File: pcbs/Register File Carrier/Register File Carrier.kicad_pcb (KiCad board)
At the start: 2 copper layers, 4 parts, among them J1001 Conn_02x20_Odd_Even, J1002 Conn_02x20_Odd_Even

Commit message: Roughing a little more out
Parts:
- added J2003: ~, BoardEdgeConnectors:TE-5530843-4-Mount, F.Cu at (151.1, 118.7)
- added J2004: ~, BoardEdgeConnectors:TE-5530843-4-Mount, F.Cu at (148.6, 70.5)
- added U2001: 74AHC04, Package_SO:SOIC-14_3.9x8.7mm_P1.27mm, F.Cu at (109.2, 127.0)
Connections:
- J1001 pad 10: /A7 -> /Connector Block/A7
- J1001 pad 11: /A8 -> /Connector Block/A8
- J1001 pad 12: /A9 -> /Connector Block/A9
- J1001 pad 13: /A10 -> /Connector Block/A10
- J1001 pad 14: /A11 -> /Connector Block/A11
- J1001 pad 15: /A12 -> /Connector Block/A12
- J1001 pad 16: /A13 -> /Connector Block/A13
- J1001 pad 17: /A14 -> /Connector Block/A14
- J1001 pad 18: /A15 -> /Connector Block/A15
- J1001 pad 19: /B0 -> /Connector Block/B0
- J1001 pad 20: /B1 -> /Connector Block/B1
- J1001 pad 21: /B2 -> /Connector Block/B2
- J1001 pad 22: /B3 -> /Connector Block/B3
- J1001 pad 23: /B4 -> /Connector Block/B4
- J1001 pad 24: /B5 -> /Connector Block/B5
- J1001 pad 25: /B6 -> /Connector Block/B6
- J1001 pad 26: /B7 -> /Connector Block/B7
- J1001 pad 27: /B8 -> /Connector Block/B8
- J1001 pad 28: /B9 -> /Connector Block/B9
- J1001 pad 29: /B10 -> /Connector Block/B10
- J1001 pad 3: /A0 -> /Connector Block/A0
- J1001 pad 30: /B11 -> /Connector Block/B11
- J1001 pad 31: /B12 -> /Connector Block/B12
- J1001 pad 32: /B13 -> /Connector Block/B13
- J1001 pad 33: /B14 -> /Connector Block/B14
- J1001 pad 34: /B15 -> /Connector Block/B15
- J1001 pad 4: /A1 -> /Connector Block/A1
- J1001 pad 5: /A2 -> /Connector Block/A2
- J1001 pad 6: /A3 -> /Connector Block/A3
- J1001 pad 7: /A4 -> /Connector Block/A4
- J1001 pad 8: /A5 -> /Connector Block/A5
- J1001 pad 9: /A6 -> /Connector Block/A6
- J1002 pad 1: /C0 -> /Connector Block/C0
- J1002 pad 10: /C9 -> /Connector Block/C9
- J1002 pad 11: /C10 -> /Connector Block/C10
- J1002 pad 12: /C11 -> /Connector Block/C11
- J1002 pad 13: /C12 -> /Connector Block/C12
- J1002 pad 14: /C13 -> /Connector Block/C13
- J1002 pad 15: /C14 -> /Connector Block/C14
- J1002 pad 16: /C15 -> /Connector Block/C15
- J1002 pad 2: /C1 -> /Connector Block/C1
- J1002 pad 3: /C2 -> /Connector Block/C2
- J1002 pad 4: /C3 -> /Connector Block/C3
- J1002 pad 5: /C4 -> /Connector Block/C4
- J1002 pad 6: /C5 -> /Connector Block/C5
- J1002 pad 7: /C6 -> /Connector Block/C6
- J1002 pad 8: /C7 -> /Connector Block/C7
- J1002 pad 9: /C8 -> /Connector Block/C8

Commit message: Working on register selectors
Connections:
- J1002 pad 21: /I4 -> /Connector Block/R_{A}0
- J1002 pad 22: /I5 -> /Connector Block/R_{A}1
- J1002 pad 23: /I6 -> /Connector Block/R_{A}2
- J1002 pad 24: /I7 -> /Connector Block/R_{A}3

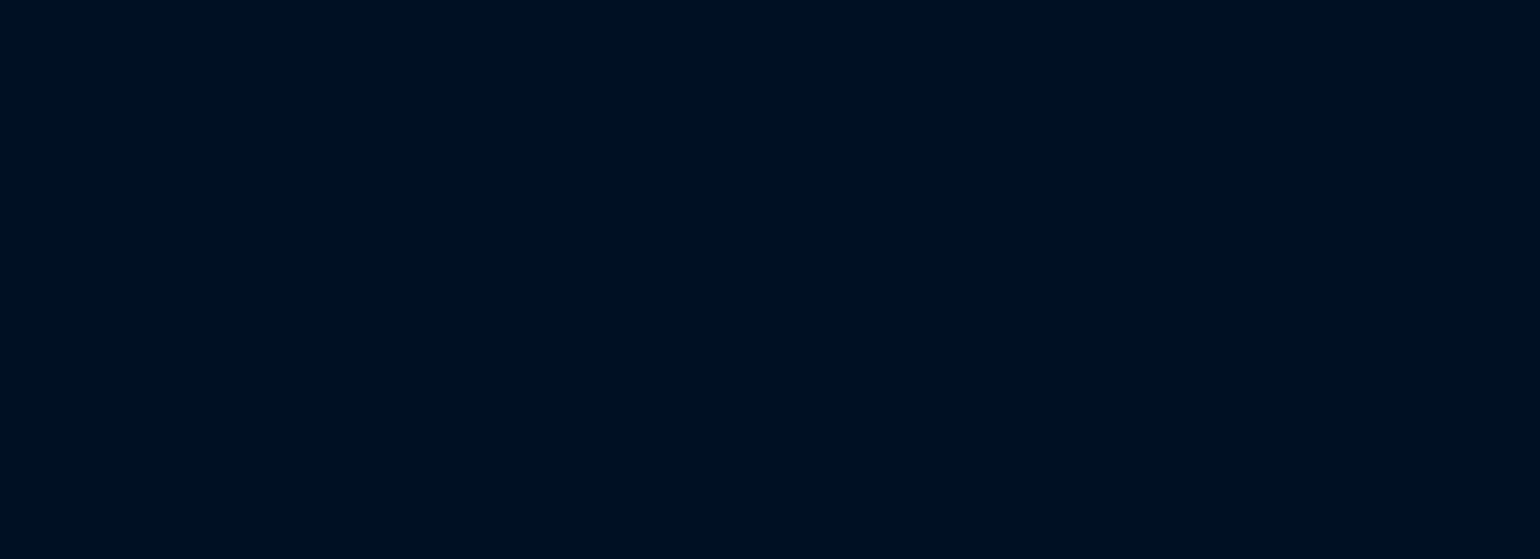
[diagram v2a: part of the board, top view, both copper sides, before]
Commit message: Thinking some things through
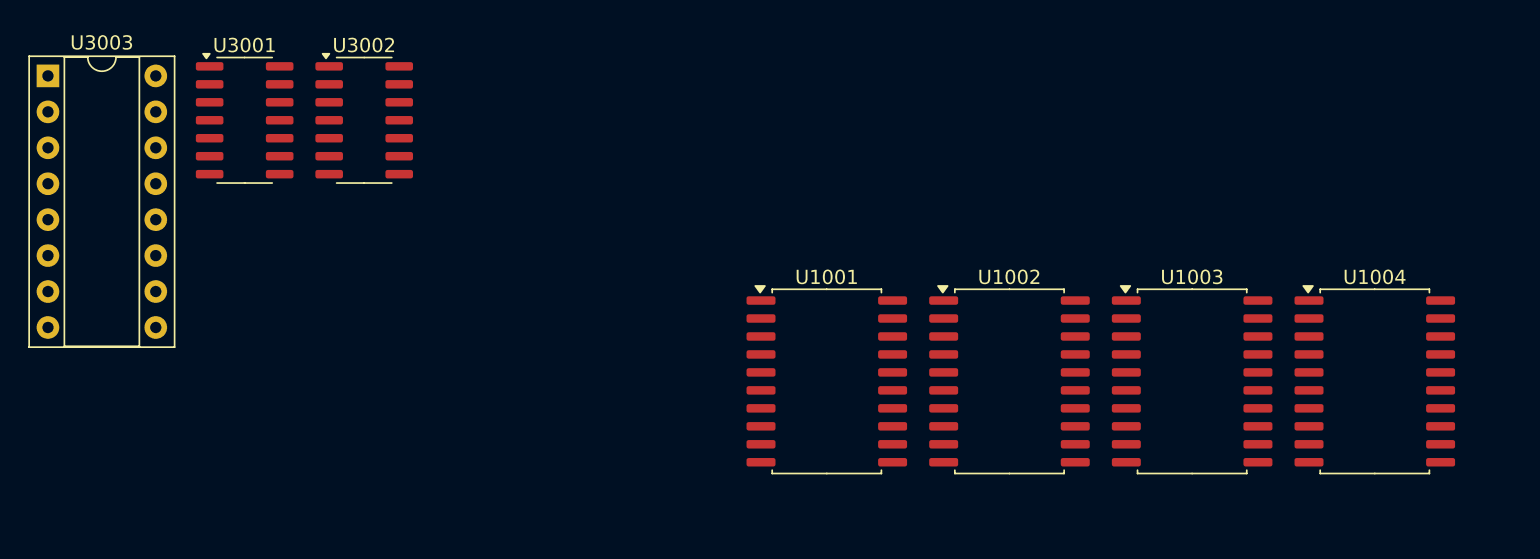
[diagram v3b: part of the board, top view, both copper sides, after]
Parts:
- added U1001: 74HC245, Package_SO:SOIC-20W_7.5x12.8mm_P1.27mm, F.Cu at (74.7, 40.0)
- added U1002: 74HC245, Package_SO:SOIC-20W_7.5x12.8mm_P1.27mm, F.Cu at (87.6, 40.0)
- added U1003: 74HC245, Package_SO:SOIC-20W_7.5x12.8mm_P1.27mm, F.Cu at (100.5, 40.0)
- added U1004: 74HC245, Package_SO:SOIC-20W_7.5x12.8mm_P1.27mm, F.Cu at (113.5, 40.0)
- added U3001: 74HC14, Package_SO:SOIC-14_3.9x8.7mm_P1.27mm, F.Cu at (33.6, 21.6)
- added U3002: 74HC08, Package_SO:SOIC-14_3.9x8.7mm_P1.27mm, F.Cu at (42.0, 21.6)
- added U3003: 74HC138, Package_DIP:DIP-16_W7.62mm_Socket, F.Cu at (19.7, 18.4)
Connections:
- J1001 pad 10: /Connector Block/A7 -> /Ao7
- J1001 pad 11: /Connector Block/A8 -> /Ao8
- J1001 pad 12: /Connector Block/A9 -> /Ao9
- J1001 pad 13: /Connector Block/A10 -> /Ao10
- J1001 pad 14: /Connector Block/A11 -> /Ao11
- J1001 pad 15: /Connector Block/A12 -> /Ao12
- J1001 pad 16: /Connector Block/A13 -> /Ao13
- J1001 pad 17: /Connector Block/A14 -> /Ao14
- J1001 pad 18: /Connector Block/A15 -> /Ao15
- J1001 pad 19: /Connector Block/B0 -> /Bo0
- J1001 pad 20: /Connector Block/B1 -> /Bo1
- J1001 pad 21: /Connector Block/B2 -> /Bo2
- J1001 pad 22: /Connector Block/B3 -> /Bo3
- J1001 pad 23: /Connector Block/B4 -> /Bo4
- J1001 pad 24: /Connector Block/B5 -> /Bo5
- J1001 pad 25: /Connector Block/B6 -> /Bo6
- J1001 pad 26: /Connector Block/B7 -> /Bo7
- J1001 pad 27: /Connector Block/B8 -> /Bo8
- J1001 pad 28: /Connector Block/B9 -> /Bo9
- J1001 pad 29: /Connector Block/B10 -> /Bo10
- J1001 pad 3: /Connector Block/A0 -> /Ao0
- J1001 pad 30: /Connector Block/B11 -> /Bo11
- J1001 pad 31: /Connector Block/B12 -> /Bo12
- J1001 pad 32: /Connector Block/B13 -> /Bo13
- J1001 pad 33: /Connector Block/B14 -> /Bo14
- J1001 pad 34: /Connector Block/B15 -> /Bo15
- J1001 pad 4: /Connector Block/A1 -> /Ao1
- J1001 pad 5: /Connector Block/A2 -> /Ao2
- J1001 pad 6: /Connector Block/A3 -> /Ao3
- J1001 pad 7: /Connector Block/A4 -> /Ao4
- J1001 pad 8: /Connector Block/A5 -> /Ao5
- J1001 pad 9: /Connector Block/A6 -> /Ao6
- J1002 pad 25: /I8 -> /Connector Block/R_{B}0
- J1002 pad 26: /I9 -> /Connector Block/R_{B}1
- J1002 pad 27: /I10 -> /Connector Block/R_{B}2
- J1002 pad 28: /I11 -> /Connector Block/R_{B}3
- J1002 pad 29: /I12 -> /Connector Block/R_{C}0
- J1002 pad 30: /I13 -> /Connector Block/R_{C}1
- J1002 pad 31: /I14 -> /Connector Block/R_{C}2
- J1002 pad 32: /I15 -> /Connector Block/R_{C}3

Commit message: Adding some more bits
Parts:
- added U3004: 74HC08, Package_SO:SOIC-14_3.9x8.7mm_P1.27mm, F.Cu at (39.4, 36.8)
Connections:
- J1002 pad 17: /I0 -> /Enabler/I0
- J1002 pad 18: /I1 -> /Enabler/I1
- J1002 pad 19: /I2 -> /Enabler/I2
- J1002 pad 20: /I3 -> /Enabler/I3
- J1002 pad 35: /Cycle2 -> /Enabler/Cycle2
- J1002 pad 36: /Cycle3 -> /Enabler/Cycle3
- J1002 pad 37: /Cycle4 -> /Enabler/Cycle4
- U3001 pad 3: GND -> /Enabler/~{Set}
- U3001 pad 4: unconnected-(U3001-Pad4) -> /Connector Block/~{Active}
- U3001 pad 8: Net-(U3001-Pad8) -> unconnected-(U3001-Pad8)
- U3001 pad 9: Net-(U3001-Pad9) -> GND
- U3002 pad 3: Net-(U3001-Pad9) -> Net-(U3002-Pad3)
- U3002 pad 4: Net-(U3001-Pad8) -> Net-(U3002-Pad3)
- U3003 pad 1: unconnected-(U3003-A0-Pad1) -> /Enabler/I0
- U3003 pad 10: unconnected-(U3003-~{Y5}-Pad10) -> /Enabler/~{BranchZero}
- U3003 pad 11: unconnected-(U3003-~{Y4}-Pad11) -> /Enabler/~{LoadPC}
- U3003 pad 12: unconnected-(U3003-~{Y3}-Pad12) -> /Enabler/~{StoreW}
- U3003 pad 13: unconnected-(U3003-~{Y2}-Pad13) -> /Enabler/~{StoreB}
- U3003 pad 14: unconnected-(U3003-~{Y1}-Pad14) -> /Enabler/~{LoadW}
- U3003 pad 15: unconnected-(U3003-~{Y0}-Pad15) -> /Enabler/~{LoadB}
- U3003 pad 16: unconnected-(U3003-VCC-Pad16) -> +5V
- U3003 pad 2: unconnected-(U3003-A1-Pad2) -> /Enabler/I1
- U3003 pad 3: unconnected-(U3003-A2-Pad3) -> /Enabler/I2
- U3003 pad 4: unconnected-(U3003-~{E0}-Pad4) -> /Enabler/~{Enable}
- U3003 pad 6: unconnected-(U3003-E2-Pad6) -> /Enabler/I3
- U3003 pad 7: unconnected-(U3003-~{Y7}-Pad7) -> /Enabler/~{Set}
- U3003 pad 8: unconnected-(U3003-GND-Pad8) -> GND
- U3003 pad 9: unconnected-(U3003-~{Y6}-Pad9) -> /Enabler/~{Halt}

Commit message: Starting to route
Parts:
- removed U1001, U1002, U1003, U1004: 74HC245, Package_SO:SOIC-20W_7.5x12.8mm_P1.27mm
- added U4001: 74HC245, Package_SO:SOIC-20W_7.5x12.8mm_P1.27mm, F.Cu at (249.8, 131.4)
- added U4002: 74HC245, Package_SO:SOIC-20W_7.5x12.8mm_P1.27mm, F.Cu at (264.6, 134.6)
- added U5001: 74HC245, Package_SO:SOIC-20W_7.5x12.8mm_P1.27mm, F.Cu at (275.8, 149.2)
- added U5002: 74HC245, Package_SO:SOIC-20W_7.5x12.8mm_P1.27mm, F.Cu at (289.4, 156.8)
- moved J2001 97.7 mm to (101.6, 101.6), turned to -90 degrees
- moved J2004 85.8 mm to (228.6, 101.6), turned to -90 degrees
- moved U2001 75.5 mm to (165.1, 76.2), turned to 0 degrees
- moved J2002 44.2 mm to (139.7, 101.6), turned to -90 degrees
- moved J2003 42.9 mm to (190.5, 101.6), turned to -90 degrees
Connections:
- U3001 pad 2: /Enabler/~{Enable} -> /Connector Block/~{Active}
- U3001 pad 4: /Connector Block/~{Active} -> /Enabler/~{AB_{Enable}}
- U3003 pad 4: /Enabler/~{Enable} -> /Connector Block/~{Active}
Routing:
- net /Connector Block/A3: track 0.00 -> 272.3 mm, vias 0 -> 2
- net /Connector Block/A0: track 0.00 -> 250.1 mm, vias 0 -> 2
- net /Connector Block/A2: track 0.00 -> 236.7 mm, vias 0 -> 2
- net /Connector Block/B0: track 0.00 -> 234.8 mm, vias 0 -> 2
- net /Connector Block/A4: track 0.00 -> 232.3 mm, vias 0 -> 2
- net /Connector Block/B2: track 0.00 -> 229.1 mm, vias 0 -> 2
- net /Connector Block/A6: track 0.00 -> 227.9 mm, vias 0 -> 2
- net /Connector Block/C0: track 0.00 -> 226.0 mm, vias 0 -> 2
- net /Connector Block/B4: track 0.00 -> 224.7 mm, vias 0 -> 2
- net /Connector Block/A12: track 0.00 -> 220.9 mm, vias 0 -> 2
- net /Connector Block/A1: track 0.00 -> 218.3 mm, vias 0 -> 2
- net /Connector Block/B1: track 0.00 -> 215.8 mm, vias 0 -> 2
- net /Connector Block/A7: track 0.00 -> 213.9 mm, vias 0 -> 2
- net /Connector Block/A8: track 0.00 -> 213.3 mm, vias 0 -> 2
- net /Connector Block/B3: track 0.00 -> 212.6 mm, vias 0 -> 2
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
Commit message: Rethinking layout
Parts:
- moved J1002 249.6 mm to (279.4, 165.1)
- moved J1001 235.5 mm to (279.4, 101.6)
- moved U5002 48.1 mm to (248.9, 182.9)
- moved U5001 32.6 mm to (248.9, 167.6)
- moved U4002 23.7 mm to (248.9, 152.4)
- moved U4001 5.78 mm to (248.9, 137.2)
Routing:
- net /Connector Block/C6: track 210.7 -> 34.8 mm, vias 2 -> 0
- net /Connector Block/C15: track 175.8 -> 5.61 mm, vias 2 -> 0
- net /Connector Block/C7: track 203.7 -> 34.8 mm, vias 2 -> 0
- net /Connector Block/C4: track 185.3 -> 24.0 mm, vias 2 -> 0
- net /Connector Block/C5: track 205.1 -> 54.7 mm, vias 2 -> 0
- net /Connector Block/C8: track 198.0 -> 67.2 mm, vias 2 -> 0
- net /Connector Block/C10: track 193.6 -> 85.6 mm, vias 2 -> 0
- net /Connector Block/C12: track 189.1 -> 81.8 mm, vias 2 -> 0
- net /Connector Block/C14: track 184.7 -> 78.0 mm, vias 2 -> 0
- net /Connector Block/C1: track 190.4 -> 294.5 mm
- net /Connector Block/C9: track 185.3 -> 90.7 mm, vias 2 -> 0
- net /Connector Block/C13: track 177.1 -> 88.2 mm, vias 2 -> 0
- net /Connector Block/C11: track 175.8 -> 86.9 mm, vias 2 -> 0
- net /Connector Block/B12: track 175.8 -> 264.5 mm
- net /Connector Block/B10: track 179.6 -> 266.4 mm
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
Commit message: Thinking some routing
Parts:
- moved J1002 25.5 mm to (281.9, 190.5)
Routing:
- net /Connector Block/C4: track 24.0 -> 302.2 mm, vias 0 -> 2
- net /Connector Block/C15: track 5.61 -> 277.5 mm, vias 0 -> 2
- net /Connector Block/C6: track 34.8 -> 300.2 mm, vias 0 -> 2
- net /Connector Block/C7: track 34.8 -> 292.6 mm, vias 0 -> 2
- net /Connector Block/C5: track 54.7 -> 293.4 mm, vias 0 -> 2
- net /Connector Block/C8: track 67.2 -> 288.2 mm, vias 0 -> 2
- net /Connector Block/C14: track 78.0 -> 282.5 mm, vias 0 -> 2
- net /Connector Block/C12: track 81.8 -> 284.4 mm, vias 0 -> 2
- net /Connector Block/C10: track 85.6 -> 286.3 mm, vias 0 -> 2
- net /Connector Block/C13: track 88.2 -> 280.6 mm, vias 0 -> 2
- net /Connector Block/C11: track 86.9 -> 276.1 mm, vias 0 -> 2
- net /Connector Block/C9: track 90.7 -> 276.8 mm, vias 0 -> 2
- net /Connector Block/C2: track 155.5 -> 304.1 mm, vias 1 -> 2
- net /Connector Block/C3: track 245.0 -> 293.9 mm, vias 1 -> 2

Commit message: Lots of routing
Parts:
- moved U3003 248.7 mm to (262.9, 70.5)
- moved U3004 238.5 mm to (268.6, 102.9)
- moved U3002 231.7 mm to (259.0, 102.9)
- moved U3001 230.7 mm to (249.5, 102.9)
- moved J1001 13.7 mm to (284.5, 114.3)
- moved J1002 2.54 mm to (284.5, 190.5)
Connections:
- U2001 pad 10: unconnected-(U2001-Pad10) -> /Connector Block/~{R_{B}3}
- U2001 pad 11: GND -> /Connector Block/R_{B}3
- U2001 pad 3: /Connector Block/R_{B}3 -> GND
- U2001 pad 4: /Connector Block/~{R_{B}3} -> unconnected-(U2001-Pad4)
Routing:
- net /Connector Block/R_{A}2: track 0.00 -> 555.4 mm, vias 0 -> 6
- net /Connector Block/R_{B}1: track 0.00 -> 542.6 mm, vias 0 -> 6
- net /Connector Block/R_{A}1: track 0.00 -> 540.1 mm, vias 0 -> 6
- net /Connector Block/R_{B}2: track 0.00 -> 537.6 mm, vias 0 -> 6
- net /Connector Block/R_{B}0: track 0.00 -> 532.5 mm, vias 0 -> 6
- net /Connector Block/R_{A}0: track 0.00 -> 530.0 mm, vias 0 -> 6
- net /Connector Block/R_{C}2: track 0.00 -> 519.2 mm, vias 0 -> 6
- net /Connector Block/R_{B}3: track 0.00 -> 514.2 mm, vias 0 -> 6
- net /Connector Block/R_{C}1: track 0.00 -> 494.3 mm, vias 0 -> 6
- net /Connector Block/R_{C}0: track 0.00 -> 484.9 mm, vias 0 -> 6
- net /Connector Block/R_{A}3: track 0.00 -> 471.0 mm, vias 0 -> 7
- net /Connector Block/R_{C}3: track 0.00 -> 426.6 mm, vias 0 -> 6
- net /Connector Block/~{Active}: track 0.00 -> 295.7 mm, vias 0 -> 4
- net /Connector Block/CLK: track 0.00 -> 286.8 mm, vias 0 -> 4
- net /Connector Block/~{R_{A}3}: track 0.00 -> 208.2 mm, vias 0 -> 4
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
